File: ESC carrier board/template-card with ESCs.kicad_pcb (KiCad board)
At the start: 2 copper layers, 111.8 x 83 mm, 18 parts, among them J3 Conn_01x04_Pin, J4 Conn_01x04_Pin, J5 Conn_01x04_Pin, U2 ESC, U4 ESC, U6 ESC

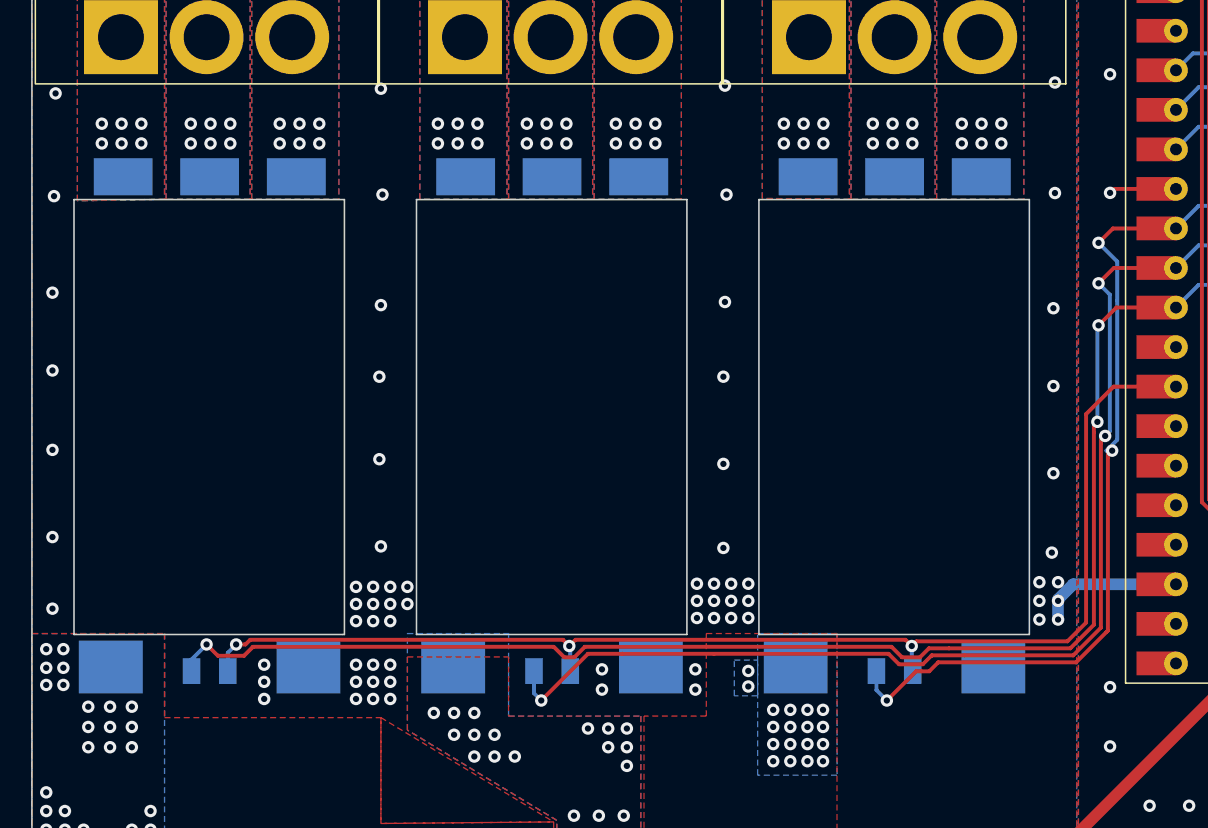
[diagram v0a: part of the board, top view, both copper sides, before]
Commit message: Modified Board for easier ESC mounting
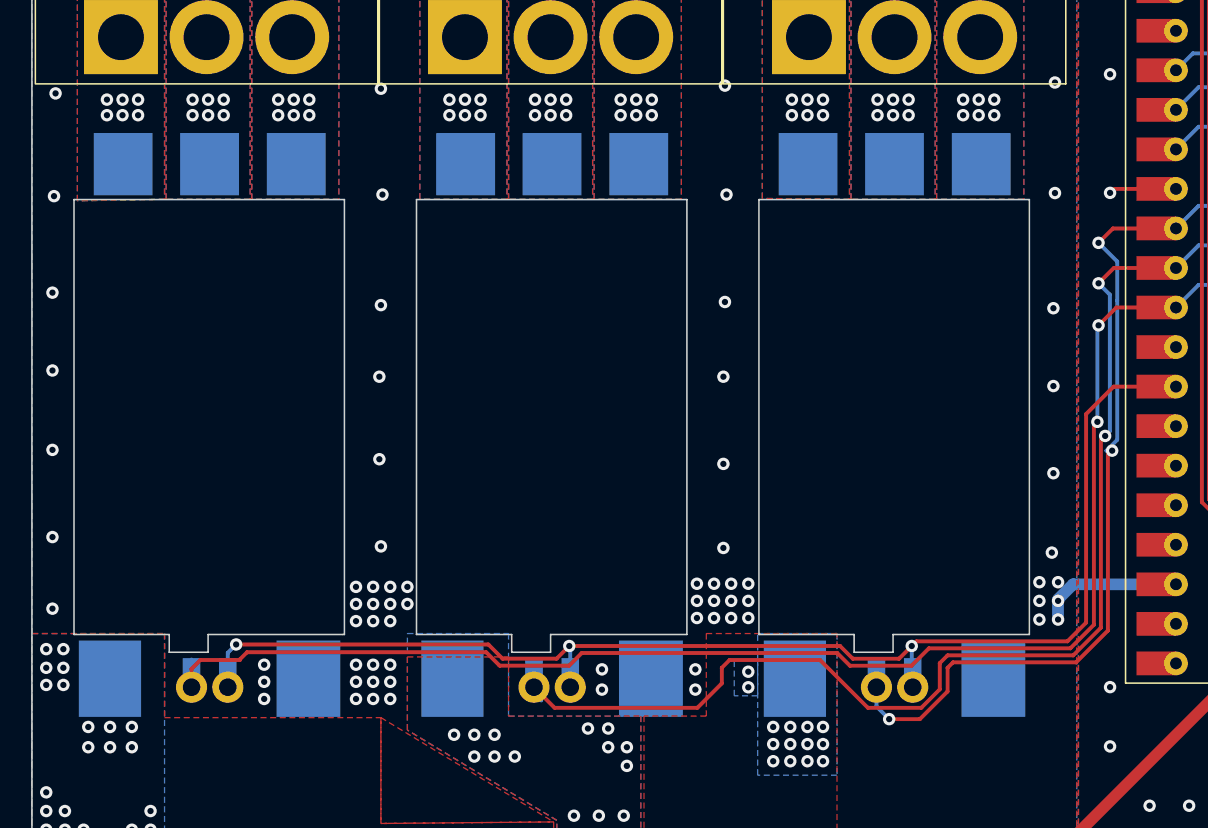
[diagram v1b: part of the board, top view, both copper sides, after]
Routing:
- net /sGP7: track 98.5 -> 103.3 mm, vias 4 -> 3
- net /sGP6: track 79.7 -> 82.2 mm
- net /sGP8: track 116.0 -> 117.1 mm, vias 4 -> 3
- net sGND: track 97.7 -> 98.5 mm
- net /12v3: vias 18 -> 14
- net /12v2: vias 21 -> 17
- net /12v1: vias 24 -> 21
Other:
- outline, holes or cut-outs redrawn

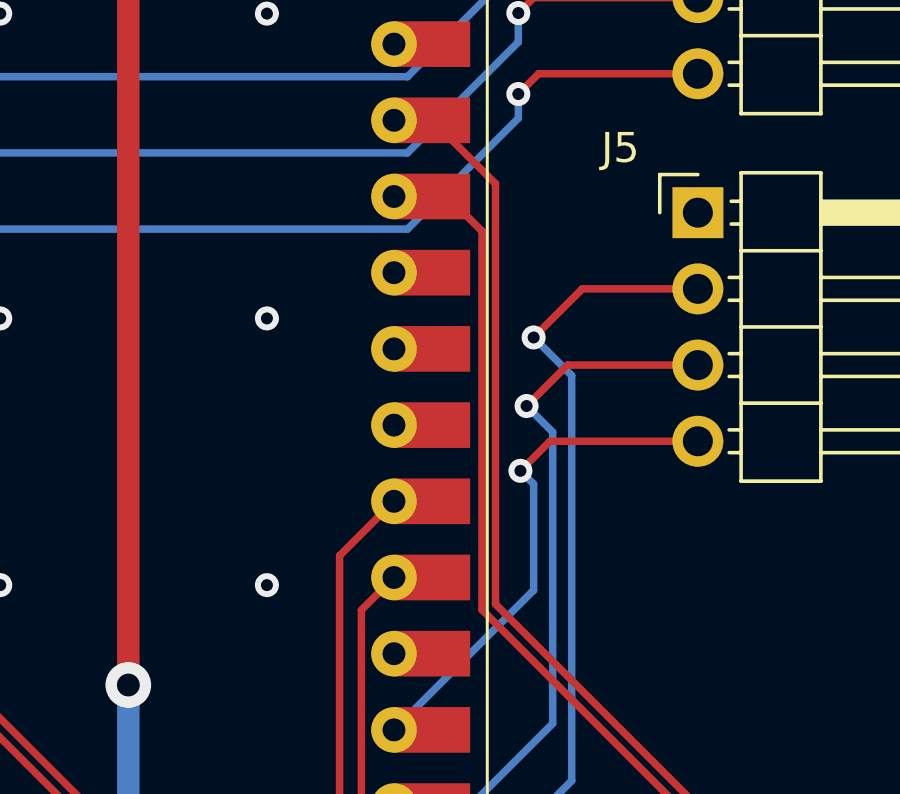
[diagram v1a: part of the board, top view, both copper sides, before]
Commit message: Shorted I2C
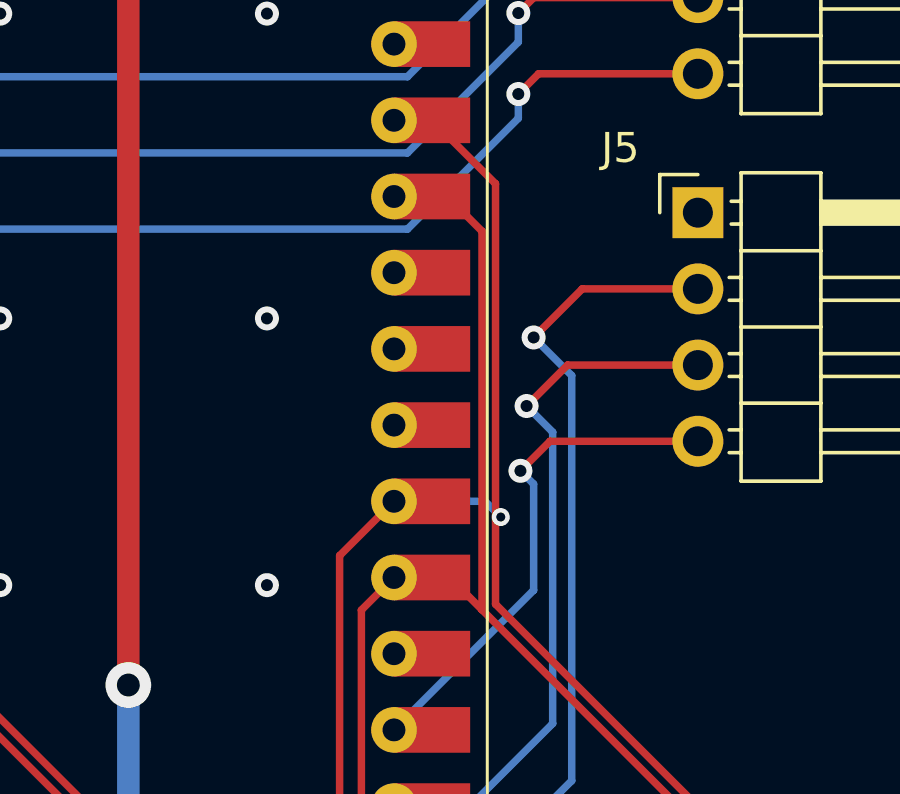
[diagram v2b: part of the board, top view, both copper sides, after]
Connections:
- JP1 pad 2: SDA1 -> SDA0
- JP2 pad 2: SCL1 -> SCL0
- U7 pad 31: SDA1 -> SDA0
- U7 pad 32: SCL1 -> SCL0
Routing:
- net SCL0: track 41.5 -> 95.0 mm, vias 3 -> 4
- net SDA0: track 43.7 -> 95.1 mm
- net SCL1: track 49.5 -> 0.00 mm
- net SDA1: track 48.0 -> 0.00 mm
